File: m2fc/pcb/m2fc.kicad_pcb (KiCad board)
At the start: 4 copper layers, 100 x 70 mm, 348 parts, among them IC101 ADP3335, IC102 STM32F405VGT, IC103 ADP3335, IC201 AD8226, IC202 AD8656, IC203 AD8541, IC204 AD8226, IC205 AD8656, IC206 AD8541, IC207 AD8226, IC208 AD8656, IC209 AD8541, IC301 ADXL375, IC302 ADXL345, IC303 MS5611-01BA03, IC304 HMC5883L, IC305 L3G4200D, IC401 ADuM5201, IC402 ADuM1201, IC601 AD8495, IC602 AD8656, IC603 AD8495, IC604 AD8656, IC605 AD8495, IC606 AD8656, P101 CONN_2, P102 CONN_2, P103 CONN_2, P104 SWD, P201 CONN_4, P202 CONN_4, P203 CONN_4, P401 CONN_4, P402 CONN_2, P403 CONN_4, P501 CONN_2, P502 CONN_2, P503 CONN_2, P601 CONN_2, P602 CONN_2, P603 CONN_2, Q501 MOSFET_P, Q502 MOSFET_N, Q503 MOSFET_P, Q504 MOSFET_N, Q505 MOSFET_P, Q506 MOSFET_N, U106 MICROSD, U107 MOUNT, U108 MOUNT, U109 MOUNT, U110 MOUNT, U111 MOUNT, U112 MOUNT, X101 8M

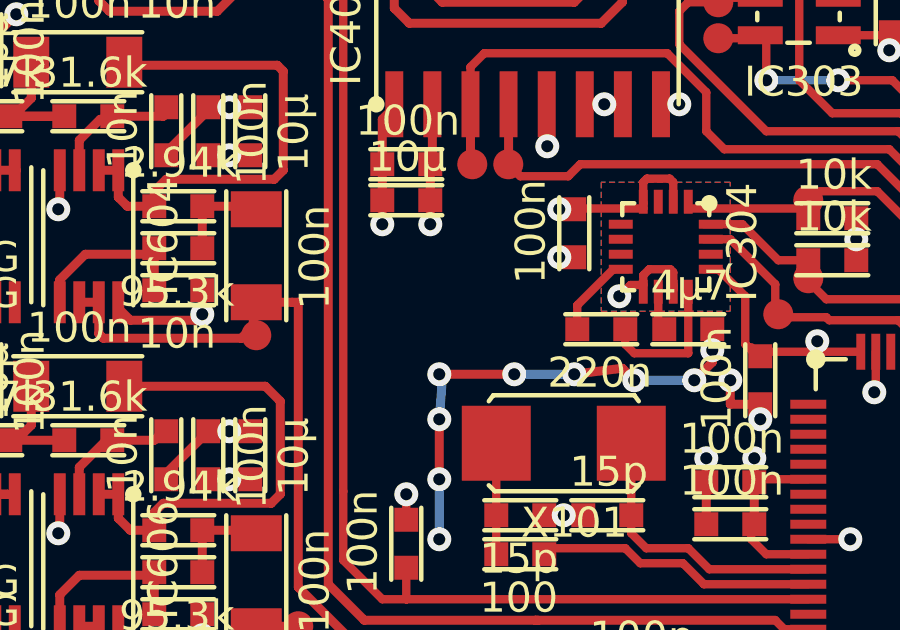
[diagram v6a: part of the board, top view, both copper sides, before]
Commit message: 3V ANALOG LED
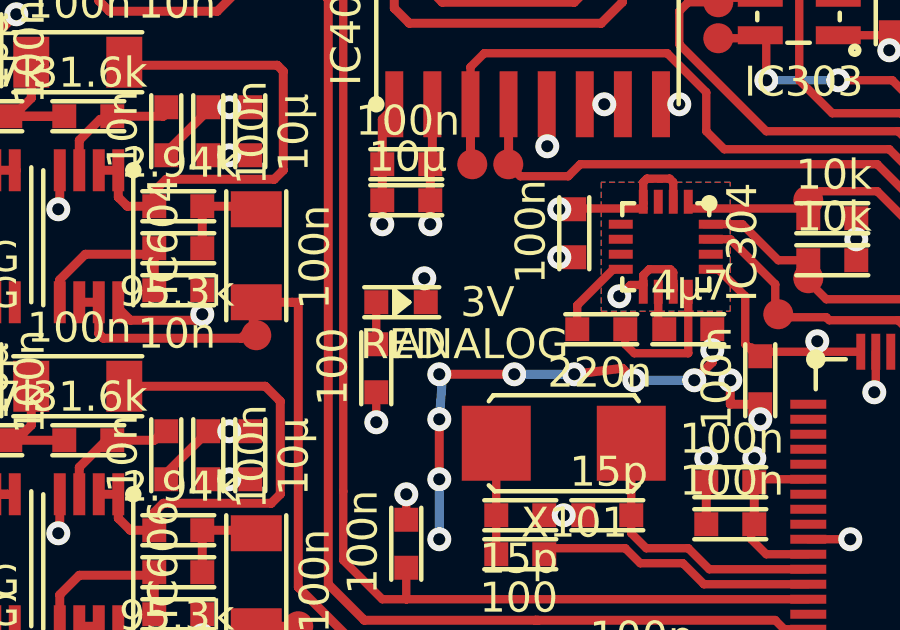
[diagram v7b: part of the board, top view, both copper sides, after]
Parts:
- added D408: RED, m2fc:LED0603, F.Cu at (81.4, 57.6)
- added R408: 100, m2fc:R0603, F.Cu at (81.4, 59.0)
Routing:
- net VAA: track 84.7 -> 87.5 mm, vias 35 -> 36
- net Net-(D408-Pad1): track 0.00 -> 1.40 mm
- net GND: track 516.3 -> 517.2 mm, vias 191 -> 192
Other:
- board text added: "3V"
- board text added: "ANALOG"
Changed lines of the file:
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@@
 (kicad_pcb (version 4) (host pcbnew "(2014-jan-25)-product")
   (general
-    (links 724)
+    (links 727)
     (no_connects 0)
     (area 47.786429 29.075 152.213572 100.375)
     (thickness 1.6)
-    (drawings 167)
-    (tracks 2564)
+    (drawings 169)
+    (tracks 2572)
     (zones 0)
-    (modules 348)
-    (nets 212)
+    (modules 350)
+    (nets 213)
   )
   (page A4)
   (layers
-    (0 F.Cu signal hide)
+    (0 F.Cu signal)
     (1 In1.Cu power hide)
     (2 In2.Cu power hide)
@@
     (34 B.Paste user hide)
     (35 F.Paste user hide)
-    (36 B.SilkS user)
+    (36 B.SilkS user hide)
     (37 F.SilkS user)
     (38 B.Mask user hide)
@@
   (net 210 "Net-(IC102-Pad61)")
   (net 211 "Net-(P102-Pad2)")
+  (net 212 "Net-(D408-Pad1)")
   (net_class Default "This is the default net class."
     (clearance 0.2)
@@
     (add_net "Net-(D404-Pad1)")
     (add_net "Net-(D405-Pad1)")
+    (add_net "Net-(D408-Pad1)")
     (add_net "Net-(D502-Pad1)")
     (add_net "Net-(D504-Pad1)")
@@
       (net 130 /SD_CD))
   )
+  (module m2fc:LED0603 (layer F.Cu)
+    (at 81.4 57.6)
+    (fp_text reference D408 (at 0.8 -1.3) (layer F.SilkS) hide
+      (effects (font (size 1 1) (thickness 0.15)))
+    )
+    (fp_text value RED (at 0.9 1.4) (layer F.SilkS)
+      (effects (font (size 1 1) (thickness 0.15)))
+    )
+    (fp_line (start -0.4 0.5) (end 2.1 0.5) (layer F.SilkS) (width 0.15))
+    (fp_line (start -0.4 -0.5) (end 2.1 -0.5) (layer F.SilkS) (width 0.15))
+    (fp_line (start 0.8 0.2) (end 0.7 0.2) (layer F.SilkS) (width 0.15))
+    (fp_line (start 0.9 0.1) (end 0.7 0.1) (layer F.SilkS) (width 0.15))
+    (fp_line (start 0.8 -0.2) (end 0.7 -0.2) (layer F.SilkS) (width 0.15))
+    (fp_line (start 0.9 -0.1) (end 0.7 -0.1) (layer F.SilkS) (width 0.15))
+    (fp_line (start 1 0) (end 0.7 0) (layer F.SilkS) (width 0.15))
+    (fp_line (start 0.6 -0.4) (end 1.1 0) (layer F.SilkS) (width 0.15))
+    (fp_line (start 1.1 0) (end 0.6 0.4) (layer F.SilkS) (width 0.15))
+    (fp_line (start 0.6 0.4) (end 0.6 -0.4) (layer F.SilkS) (width 0.15))
+    (pad 1 smd rect (at 0 0) (size 0.8 0.8) (layers F.Cu F.Paste F.Mask)
+      (net 212 "Net-(D408-Pad1)"))
+    (pad 2 smd rect (at 1.65 0) (size 0.8 0.8) (layers F.Cu F.Paste F.Mask)
+      (net 1 GND))
+  )
+  (module m2fc:R0603 (layer F.Cu)
+    (at 81.4 59 270)
+    (fp_text reference R408 (at 0.7 -1.35 270) (layer F.SilkS) hide
+      (effects (font (size 1 1) (thickness 0.15)))
+    )
+    (fp_text value 100 (at 0.75 1.45 270) (layer F.SilkS)
+      (effects (font (size 1 1) (thickness 0.15)))
+    )
+    (fp_line (start -0.4 0.5) (end 2 0.5) (layer F.SilkS) (width 0.15))
+    (fp_line (start -0.4 -0.5) (end 2 -0.5) (layer F.SilkS) (width 0.15))
+    (pad 1 smd rect (at 0 0 270) (size 0.8 0.8) (layers F.Cu F.Paste F.Mask)
+      (net 212 "Net-(D408-Pad1)"))
+    (pad 2 smd rect (at 1.6 0 270) (size 0.8 0.8) (layers F.Cu F.Paste F.Mask)
+      (net 199 VAA))
+  )
+  (gr_text ANALOG (at 82 59) (layer F.SilkS)
+    (effects (font (size 1 1) (thickness 0.25)) (justify left))
+  )
+  (gr_text 3V (at 84.2 57.6) (layer F.SilkS)
+    (effects (font (size 1 1) (thickness 0.25)) (justify left))
+  )
   (gr_circle (center 116.4 31.9) (end 116.6 31.7) (layer F.SilkS) (width 0.2))
   (gr_text "+\n-" (at 143.6 77 180) (layer B.SilkS)
@@
   (gr_arc (start 100 100) (end 84 100) (angle 180) (layer Edge.Cuts) (width 0.2))
   (segment (start 141.8 80.9) (end 141.8 81) (width 0.3) (layer F.Cu) (net 0))
+  (segment (start 83.05 57.6) (end 83.05 56.85) (width 0.28) (layer F.Cu) (net 1) (status 400000))
+  (via (at 83 56.8) (size 0.8) (drill 0.4) (layers F.Cu B.Cu) (net 1))
+  (segment (start 83.05 56.85) (end 83 56.8) (width 0.28) (layer F.Cu) (net 1))
+  (segment (start 83.2 55) (end 83.2 54.2) (width 0.3) (layer F.Cu) (net 1))
+  (segment (start 83.25 55.05) (end 83.2 55) (width 0.28) (layer F.Cu) (net 1))
+  (via (at 83.2 55) (size 0.8) (drill 0.4) (layers F.Cu B.Cu) (net 1))
   (segment (start 98.05 59.25) (end 98.05 60.55) (width 0.28) (layer F.Cu) (net 1))
   (via (at 98 60.6) (size 0.8) (drill 0.4) (layers F.Cu B.Cu) (net 1))
@@
   (segment (start 92.4 63.6) (end 92.4 62.8) (width 0.3) (layer F.Cu) (net 1))
   (segment (start 83.2 53) (end 83.2 54.2) (width 0.3) (layer F.Cu) (net 1))
-  (via (at 83.2 55) (size 0.8) (drill 0.4) (layers F.Cu B.Cu) (net 1))
-  (segment (start 83.2 54.2) (end 83.2 55) (width 0.3) (layer F.Cu) (net 1))
   (segment (start 64 78.8) (end 64.4 78.4) (width 0.3) (layer F.Cu) (net 1))
   (segment (start 64 79.1) (end 64 78.8) (width 0.3) (layer F.Cu) (net 1))
@@
   (segment (start 130.6 74.8) (end 130.1 75.3) (width 0.8) (layer F.Cu) (net 197))
   (segment (start 130.6 74.65) (end 130.6 74.8) (width 0.8) (layer F.Cu) (net 197))
+  (segment (start 79.6 61.6) (end 81.4 61.6) (width 0.28) (layer In2.Cu) (net 199))
+  (via (at 81.4 61.6) (size 0.8) (drill 0.4) (layers F.Cu B.Cu) (net 199))
+  (segment (start 81.4 61.6) (end 81.4 60.6) (width 0.28) (layer F.Cu) (net 199))
   (segment (start 67.1 39) (end 67.2 39) (width 0.3) (layer F.Cu) (net 199))
   (segment (start 68.4 39) (end 67.1 39) (width 0.3) (layer F.Cu) (net 199))
@@
   (segment (start 143 78) (end 145.9 75.1) (width 1.8) (layer F.Cu) (net 211))
   (segment (start 141.8 78) (end 142 78) (width 0.5) (layer B.Cu) (net 211))
+  (segment (start 81.4 57.6) (end 81.4 59) (width 0.28) (layer F.Cu) (net 212))
   (zone (net 1) (net_name GND) (layer In1.Cu) (hatch edge 0.508)
     (connect_pads (clearance 0.3))

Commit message: ready to go go go
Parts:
- removed G***: LOGO, m2fc:cusf_logo_full
- added U113: LOGO, m2fc:cusf_logo_full, B.Cu at (116.7, 65.2)
- added U114: LOGO, m2fc:cusf_logo_small, F.Cu at (145.9, 86.6)
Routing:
- net GND: track 517.2 -> 553.4 mm, vias 192 -> 203
- net Net-(C617-Pad2): track 6.39 -> 8.64 mm
- net Net-(C606-Pad2): track 3.74 -> 5.10 mm
- net Net-(C628-Pad2): track 4.30 -> 5.46 mm
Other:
- board text added: "PYROS"
- board text removed: "PRYOS"
